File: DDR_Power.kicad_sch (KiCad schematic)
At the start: 10 parts, among them U6 NCP114AMX250TCG

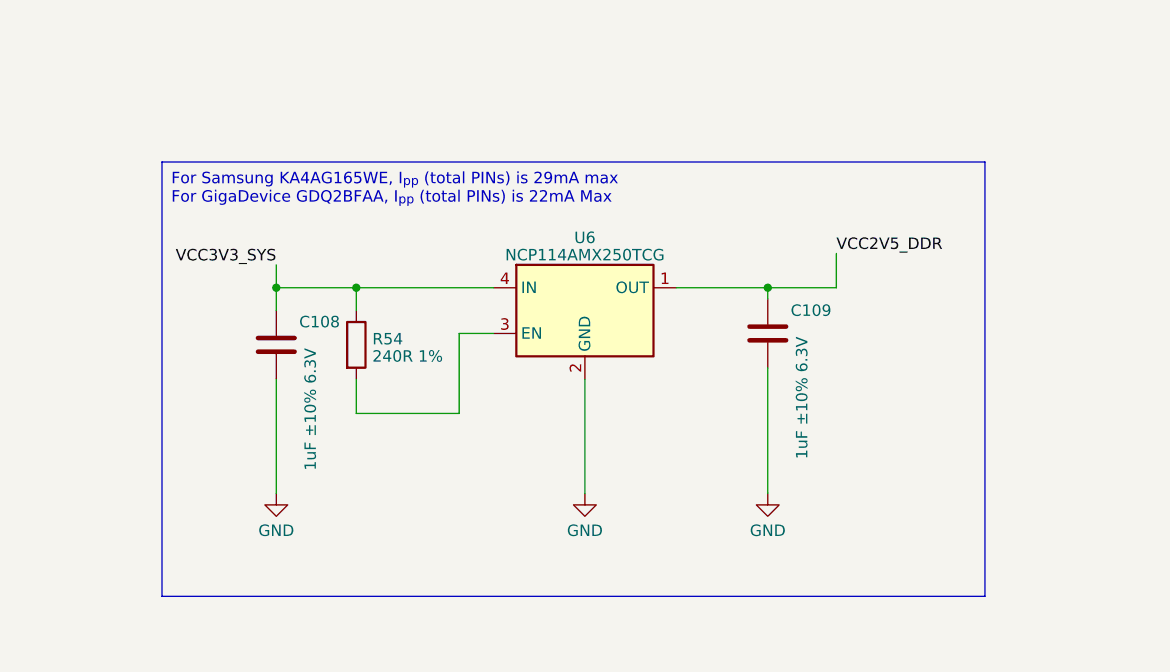
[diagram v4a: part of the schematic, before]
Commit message: added more capacitors for 2v5 output
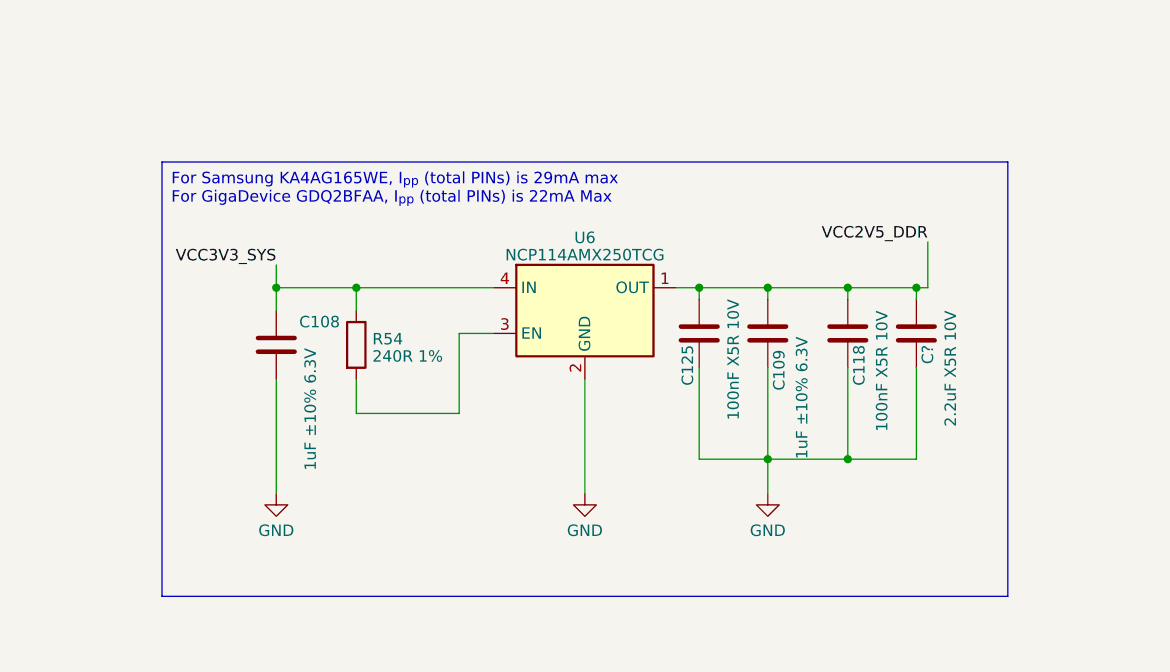
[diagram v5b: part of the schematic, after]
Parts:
- added C118, C125: 100nF X5R 10V, Capacitor_SMD:C_0402_1005Metric, symbol Device:C
- added C?: 2.2uF X5R 10V, Capacitor_SMD:C_0402_1005Metric, symbol Device:C
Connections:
- net GND: now also C118.1, C125.1, C?.1
- net VCC2V5_DDR: now also C118.2, C125.2, C?.2
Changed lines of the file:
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@@
 (kicad_sch (version 20230121) (generator eeschema)
   (paper "A4")
+  (junction (at 124.46 88.9) (diameter 0) (color 0 0 0 0)
+  )
+  (junction (at 115.57 107.95) (diameter 0) (color 0 0 0 0)
+  )
   (junction (at 69.85 88.9) (diameter 0) (color 0 0 0 0)
   )
@@
   (junction (at 222.25 100.33) (diameter 0) (color 0 0 0 0)
   )
+  (junction (at 132.08 88.9) (diameter 0) (color 0 0 0 0)
+  )
+  (junction (at 124.46 107.95) (diameter 0) (color 0 0 0 0)
+  )
   (junction (at 210.82 100.33) (diameter 0) (color 0 0 0 0)
   )
@@
   (junction (at 179.07 100.33) (diameter 0) (color 0 0 0 0)
   )
+  (junction (at 107.95 88.9) (diameter 0) (color 0 0 0 0)
+  )
   (junction (at 115.57 88.9) (diameter 0) (color 0 0 0 0)
   )
@@
     (stroke (width 0) (type default))
   )
+  (wire (pts (xy 115.57 107.95) (xy 107.95 107.95))
+    (stroke (width 0) (type default))
+  )
   (wire (pts (xy 72.39 22.86) (xy 78.74 22.86))
     (stroke (width 0) (type default))
@@
     (stroke (width 0) (type default))
   )
+  (wire (pts (xy 124.46 88.9) (xy 115.57 88.9))
+    (stroke (width 0) (type default))
+  )
   (wire (pts (xy 60.96 88.9) (xy 60.96 91.44))
     (stroke (width 0) (type default))
@@
     (stroke (width 0) (type default))
   )
+  (wire (pts (xy 124.46 107.95) (xy 115.57 107.95))
+    (stroke (width 0) (type default))
+  )
   (wire (pts (xy 81.28 93.98) (xy 85.09 93.98))
     (stroke (width 0) (type default))
@@
     (stroke (width 0) (type default))
   )
-  (wire (pts (xy 123.19 88.9) (xy 115.57 88.9))
+  (wire (pts (xy 133.35 88.9) (xy 132.08 88.9))
     (stroke (width 0) (type default))
   )
@@
     (stroke (width 0) (type default))
   )
+  (wire (pts (xy 132.08 107.95) (xy 124.46 107.95))
+    (stroke (width 0) (type default))
+  )
   (wire (pts (xy 81.28 102.87) (xy 81.28 93.98))
     (stroke (width 0) (type default))
@@
     (stroke (width 0) (type default))
   )
+  (wire (pts (xy 132.08 88.9) (xy 132.08 90.17))
+    (stroke (width 0) (type default))
+  )
+  (wire (pts (xy 115.57 107.95) (xy 115.57 111.76))
+    (stroke (width 0) (type default))
+  )
   (wire (pts (xy 199.39 100.33) (xy 199.39 104.14))
     (stroke (width 0) (type default))
@@
     (stroke (width 0) (type default))
   )
-  (wire (pts (xy 115.57 97.79) (xy 115.57 111.76))
-    (stroke (width 0) (type default))
-  )
-  (wire (pts (xy 123.19 85.09) (xy 123.19 88.9))
+  (wire (pts (xy 115.57 97.79) (xy 115.57 107.95))
+    (stroke (width 0) (type default))
+  )
+  (wire (pts (xy 107.95 88.9) (xy 107.95 90.17))
+    (stroke (width 0) (type default))
+  )
+  (wire (pts (xy 132.08 88.9) (xy 124.46 88.9))
+    (stroke (width 0) (type default))
+  )
+  (wire (pts (xy 133.35 83.82) (xy 133.35 88.9))
+    (stroke (width 0) (type default))
+  )
+  (wire (pts (xy 124.46 97.79) (xy 124.46 107.95))
     (stroke (width 0) (type default))
   )
@@
     (stroke (width 0) (type default))
   )
-  (wire (pts (xy 105.41 88.9) (xy 115.57 88.9))
+  (wire (pts (xy 132.08 97.79) (xy 132.08 107.95))
+    (stroke (width 0) (type default))
+  )
+  (wire (pts (xy 124.46 88.9) (xy 124.46 90.17))
+    (stroke (width 0) (type default))
+  )
+  (wire (pts (xy 105.41 88.9) (xy 107.95 88.9))
+    (stroke (width 0) (type default))
+  )
+  (wire (pts (xy 107.95 107.95) (xy 107.95 97.79))
     (stroke (width 0) (type default))
   )
@@
   )
   (wire (pts (xy 233.68 104.14) (xy 233.68 100.33))
+    (stroke (width 0) (type default))
+  )
+  (wire (pts (xy 107.95 88.9) (xy 115.57 88.9))
     (stroke (width 0) (type default))
   )
@@
   )
   (text_box "For Samsung KA4AG165WE, I_{pp} (total PINs) is 29mA max\nFor GigaDevice GDQ2BFAA, I_{pp} (total PINs) is 22mA Max"
-    (at 48.26 74.93 0) (size 91.44 48.26)
+    (at 48.26 74.93 0) (size 93.98 48.26)
     (stroke (width 0) (type default) (color 194 194 0 1))
     (fill (type none))
@@
     (effects (font (size 1.27 1.27)) (justify right bottom))
   )
-  (label "VCC2V5_DDR" (at 123.19 85.09 0) (fields_autoplaced)
-    (effects (font (size 1.27 1.27)) (justify left bottom))
+  (label "VCC2V5_DDR" (at 133.35 83.82 180) (fields_autoplaced)
+    (effects (font (size 1.27 1.27)) (justify right bottom))
   )
   (label "VCC3V3_SYS" (at 45.72 25.4 0) (fields_autoplaced)
@@
     )
   )
+  (symbol (lib_id "Device:C") (at 124.46 93.98 180) (unit 1)
+    (in_bom yes) (on_board yes) (dnp no)
+    (property "Reference" "C118" (at 125.73 95.25 90)
+      (effects (font (size 1.27 1.27)) (justify left))
+    )
+    (property "Value" "100nF X5R 10V" (at 128.27 91.44 90)
+      (effects (font (size 1.27 1.27)) (justify left))
+    )
+    (property "Footprint" "Capacitor_SMD:C_0402_1005Metric" (at 123.4948 90.17 0)
+      (effects (font (size 1.27 1.27)) hide)
+    )
+    (property "Datasheet" "~" (at 124.46 93.98 0)
+      (effects (font (size 1.27 1.27)) hide)
+    )
+    (property "Description" "容值: 100nF 精度: ±10% 额定电压: 10V 材质(温度系数): X5R 材质:X5R" (at 124.46 93.98 0)
+      (effects (font (size 1.27 1.27)) hide)
+    )
+    (property "LCSC" "C76934" (at 124.46 93.98 0)
+      (effects (font (size 1.27 1.27)) hide)
+    )
+    (property "Model" "GRM033R61A104KE15D" (at 124.46 93.98 0)
+      (effects (font (size 1.27 1.27)) hide)
+    )
+    (property "Vendor" "muRata(村田)" (at 124.46 93.98 0)
+      (effects (font (size 1.27 1.27)) hide)
+    )
+    (pin "1")
+    (pin "2")
+    (instances
+      (project "leaf"
+        (path "/e3b58043-16a3-43c8-9fad-9c9784eebfa4/9453ad46-b3ff-4d4e-8aa6-7cc75aa0f522/f6658df5-193a-49b6-ab60-4ac3c0bbbc45"
+          (reference "C118") (unit 1)
+        )
+        (path "/e3b58043-16a3-43c8-9fad-9c9784eebfa4/9453ad46-b3ff-4d4e-8aa6-7cc75aa0f522/43b336b1-9a2a-4a37-8b6d-a408b4dd9ca2/30476355-385f-41d9-8be0-39b5df88b3ca"
+          (reference "C118") (unit 1)
+        )
+      )
+    )
+  )
   (symbol (lib_id "Device:C") (at 222.25 107.95 0) (unit 1)
     (in_bom yes) (on_board yes) (dnp no)
@@
     )
   )
+  (symbol (lib_id "Device:C") (at 132.08 93.98 0) (mirror x) (unit 1)
+    (in_bom yes) (on_board yes) (dnp no)
+    (property "Reference" "C?" (at 133.35 95.25 90)
+      (effects (font (size 1.27 1.27)) (justify left))
+    )
+    (property "Value" "2.2uF X5R 10V" (at 135.89 91.44 90)
+      (effects (font (size 1.27 1.27)) (justify left))
+    )
+    (property "Footprint" "Capacitor_SMD:C_0402_1005Metric" (at 133.0452 90.17 0)
+      (effects (font (size 1.27 1.27)) hide)
+    )
+    (property "Datasheet" "~" (at 132.08 93.98 0)
+      (effects (font (size 1.27 1.27)) hide)
+    )
+    (property "Description" "容值: 2.2uF 精度: ±10% 额定电压: 10V 材质(温度系数): X5R" (at 132.08 93.98 0)
+      (effects (font (size 1.27 1.27)) hide)
+    )
+    (property "Model" "GRM155R61A225KE01D" (at 132.08 93.98 0)
+      (effects (font (size 1.27 1.27)) hide)
+    )
+    (property "Vendor" "muRata(村田)" (at 132.08 93.98 0)
+      (effects (font (size 1.27 1.27)) hide)
+    )
+    (pin "1")
+    (pin "2")
+    (instances
+      (project "leaf"
+        (path "/e3b58043-16a3-43c8-9fad-9c9784eebfa4/cc9fb3ac-19c3-47a8-ba7d-678b4d514ff0/46e9a7bf-8506-4399-90d8-57d007223126/587d28a9-c2cd-4fab-a2bd-304064dd6f5e"
+          (reference "C?") (unit 1)
+        )
+        (path "/e3b58043-16a3-43c8-9fad-9c9784eebfa4/cc9fb3ac-19c3-47a8-ba7d-678b4d514ff0/46e9a7bf-8506-4399-90d8-57d007223126/932d3a83-3e3a-47a2-863a-dd551f528f64"
+          (reference "C100") (unit 1)
+        )
+        (path "/e3b58043-16a3-43c8-9fad-9c9784eebfa4/9453ad46-b3ff-4d4e-8aa6-7cc75aa0f522/f6658df5-193a-49b6-ab60-4ac3c0bbbc45"
+          (reference "C187") (unit 1)
+        )
+      )
+    )
+  )
   (symbol (lib_id "power:GND") (at 115.57 111.76 0) (unit 1)
     (in_bom yes) (on_board yes) (dnp no) (fields_autoplaced)
@@
     )
   )
+  (symbol (lib_id "Device:C") (at 107.95 93.98 180) (unit 1)
+    (in_bom yes) (on_board yes) (dnp no)
+    (property "Reference" "C125" (at 106.68 95.25 90)
+      (effects (font (size 1.27 1.27)) (justify left))
+    )
+    (property "Value" "100nF X5R 10V" (at 111.76 90.17 90)
+      (effects (font (size 1.27 1.27)) (justify left))
+    )
+    (property "Footprint" "Capacitor_SMD:C_0402_1005Metric" (at 106.9848 90.17 0)
+      (effects (font (size 1.27 1.27)) hide)
+    )
+    (property "Datasheet" "~" (at 107.95 93.98 0)
+      (effects (font (size 1.27 1.27)) hide)
+    )
+    (property "Description" "容值: 100nF 精度: ±10% 额定电压: 10V 材质(温度系数): X5R 材质:X5R" (at 107.95 93.98 0)
+      (effects (font (size 1.27 1.27)) hide)
+    )
+    (property "LCSC" "C76934" (at 107.95 93.98 0)
+      (effects (font (size 1.27 1.27)) hide)
+    )
+    (property "Model" "GRM033R61A104KE15D" (at 107.95 93.98 0)
+      (effects (font (size 1.27 1.27)) hide)
+    )
+    (property "Vendor" "muRata(村田)" (at 107.95 93.98 0)
+      (effects (font (size 1.27 1.27)) hide)
+    )
+    (pin "1")
+    (pin "2")
+    (instances
+      (project "leaf"
+        (path "/e3b58043-16a3-43c8-9fad-9c9784eebfa4/9453ad46-b3ff-4d4e-8aa6-7cc75aa0f522/f6658df5-193a-49b6-ab60-4ac3c0bbbc45"
+          (reference "C125") (unit 1)
+        )
+        (path "/e3b58043-16a3-43c8-9fad-9c9784eebfa4/9453ad46-b3ff-4d4e-8aa6-7cc75aa0f522/43b336b1-9a2a-4a37-8b6d-a408b4dd9ca2/30476355-385f-41d9-8be0-39b5df88b3ca"
+          (reference "C125") (unit 1)
+        )
+      )
+    )
+  )
   (symbol (lib_id "Device:C") (at 115.57 93.98 0) (unit 1)
     (in_bom yes) (on_board yes) (dnp no)
-    (property "Reference" "C109" (at 118.11 91.44 0)
-      (effects (font (size 1.27 1.27)) (justify left))
-    )
+    (property "Reference" "C109" (at 116.84 100.33 90)
+      (effects (font (size 1.27 1.27)) (justify left))
+    )

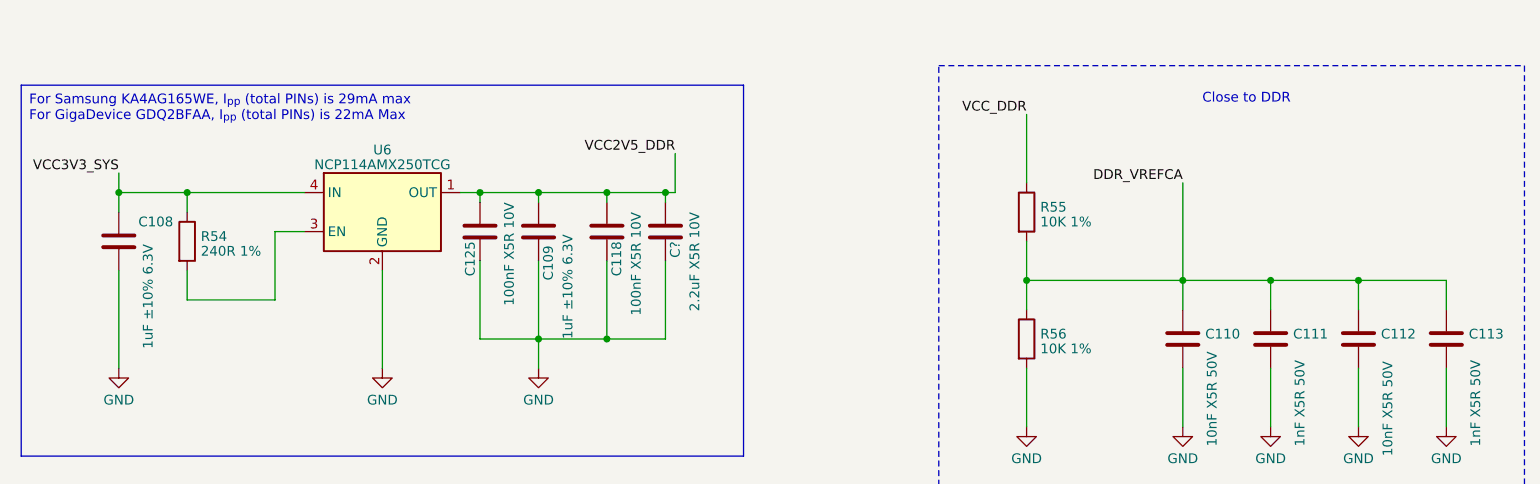
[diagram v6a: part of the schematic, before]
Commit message: resort all symbols
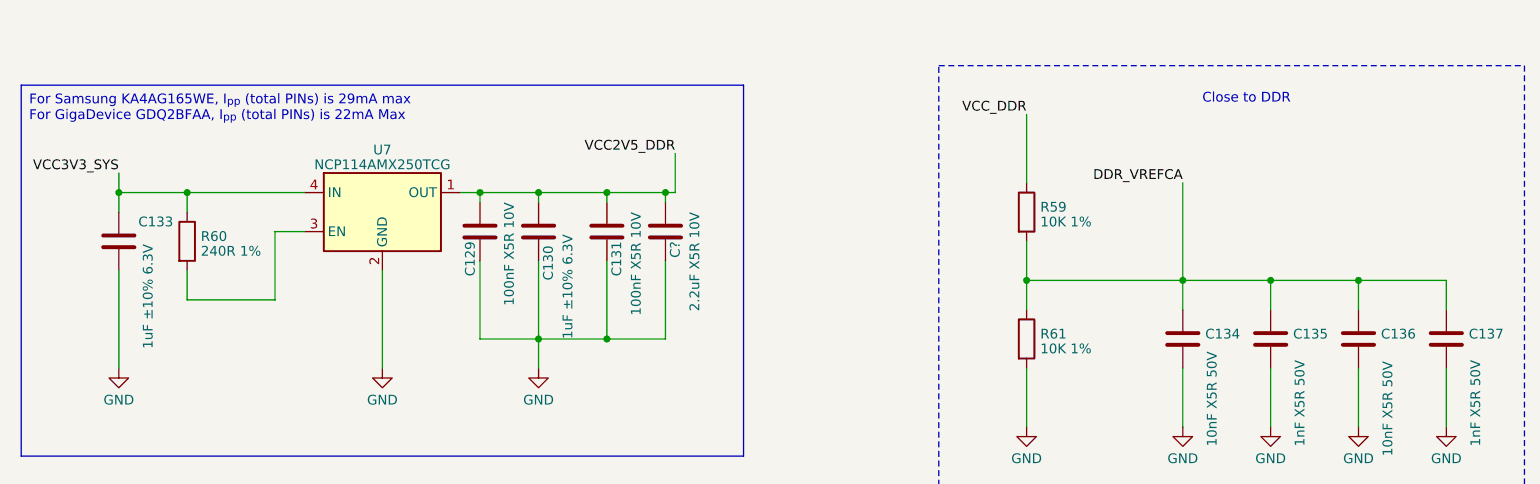
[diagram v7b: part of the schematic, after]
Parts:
- renumbered C125 to C129, C109 to C130, C118 to C131, C108 to C133, C110 to C134, C111 to C135, C112 to C136, C113 to C137, R55 to R59, R54 to R60, R56 to R61, U6 to U7

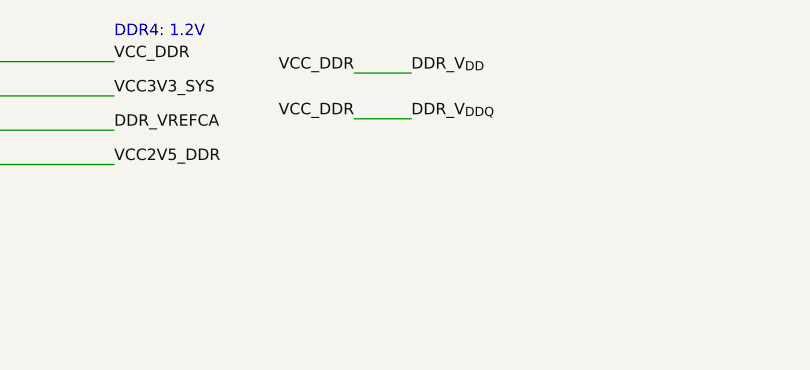
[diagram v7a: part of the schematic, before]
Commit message: remove DRC errors
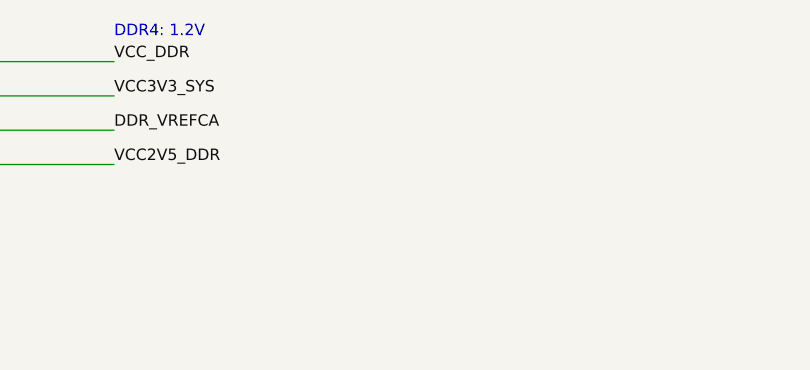
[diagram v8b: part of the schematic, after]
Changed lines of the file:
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@@
-    (stroke (width 0) (type default))
-  )
-  (wire (pts (xy 72.39 22.86) (xy 78.74 22.86))
     (stroke (width 0) (type default))
   )
@@
   )
   (wire (pts (xy 210.82 111.76) (xy 210.82 119.38))
-    (stroke (width 0) (type default))
-  )
-  (wire (pts (xy 72.39 27.94) (xy 78.74 27.94))
     (stroke (width 0) (type default))
   )
@@
     (effects (font (size 1.27 1.27)) (justify left bottom))
   )
-  (label "VCC_DDR" (at 72.39 22.86 180) (fields_autoplaced)
-    (effects (font (size 1.27 1.27)) (justify right bottom))
-  )
   (label "VCC3V3_SYS" (at 60.96 86.36 180) (fields_autoplaced)
     (effects (font (size 1.27 1.27)) (justify right bottom))
@@
     (effects (font (size 1.27 1.27)) (justify left bottom))
   )
-  (label "VCC_DDR" (at 72.39 27.94 180) (fields_autoplaced)
-    (effects (font (size 1.27 1.27)) (justify right bottom))
-  )
   (label "VCC2V5_DDR" (at 45.72 33.02 0) (fields_autoplaced)
     (effects (font (size 1.27 1.27)) (justify left bottom))
   )
-  (label "DDR_V_{DD}" (at 78.74 22.86 0) (fields_autoplaced)
-    (effects (font (size 1.27 1.27)) (justify left bottom))
-  )
-  (label "DDR_V_{DDQ}" (at 78.74 27.94 0) (fields_autoplaced)
-    (effects (font (size 1.27 1.27)) (justify left bottom))
-  )
